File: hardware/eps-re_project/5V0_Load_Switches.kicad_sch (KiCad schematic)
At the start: 28 parts, among them U1 LMV321RIYLT, U10 SI2329DS-T1-GE3, U4 INA199C1DCKR, U5 NVTFS5116PLWFTAG, U6 NVTFS5116PLWFTAG, U7 NVTFS5116PLWFTAG, U8 SI2329DS-T1-GE3, U9 SI2329DS-T1-GE3

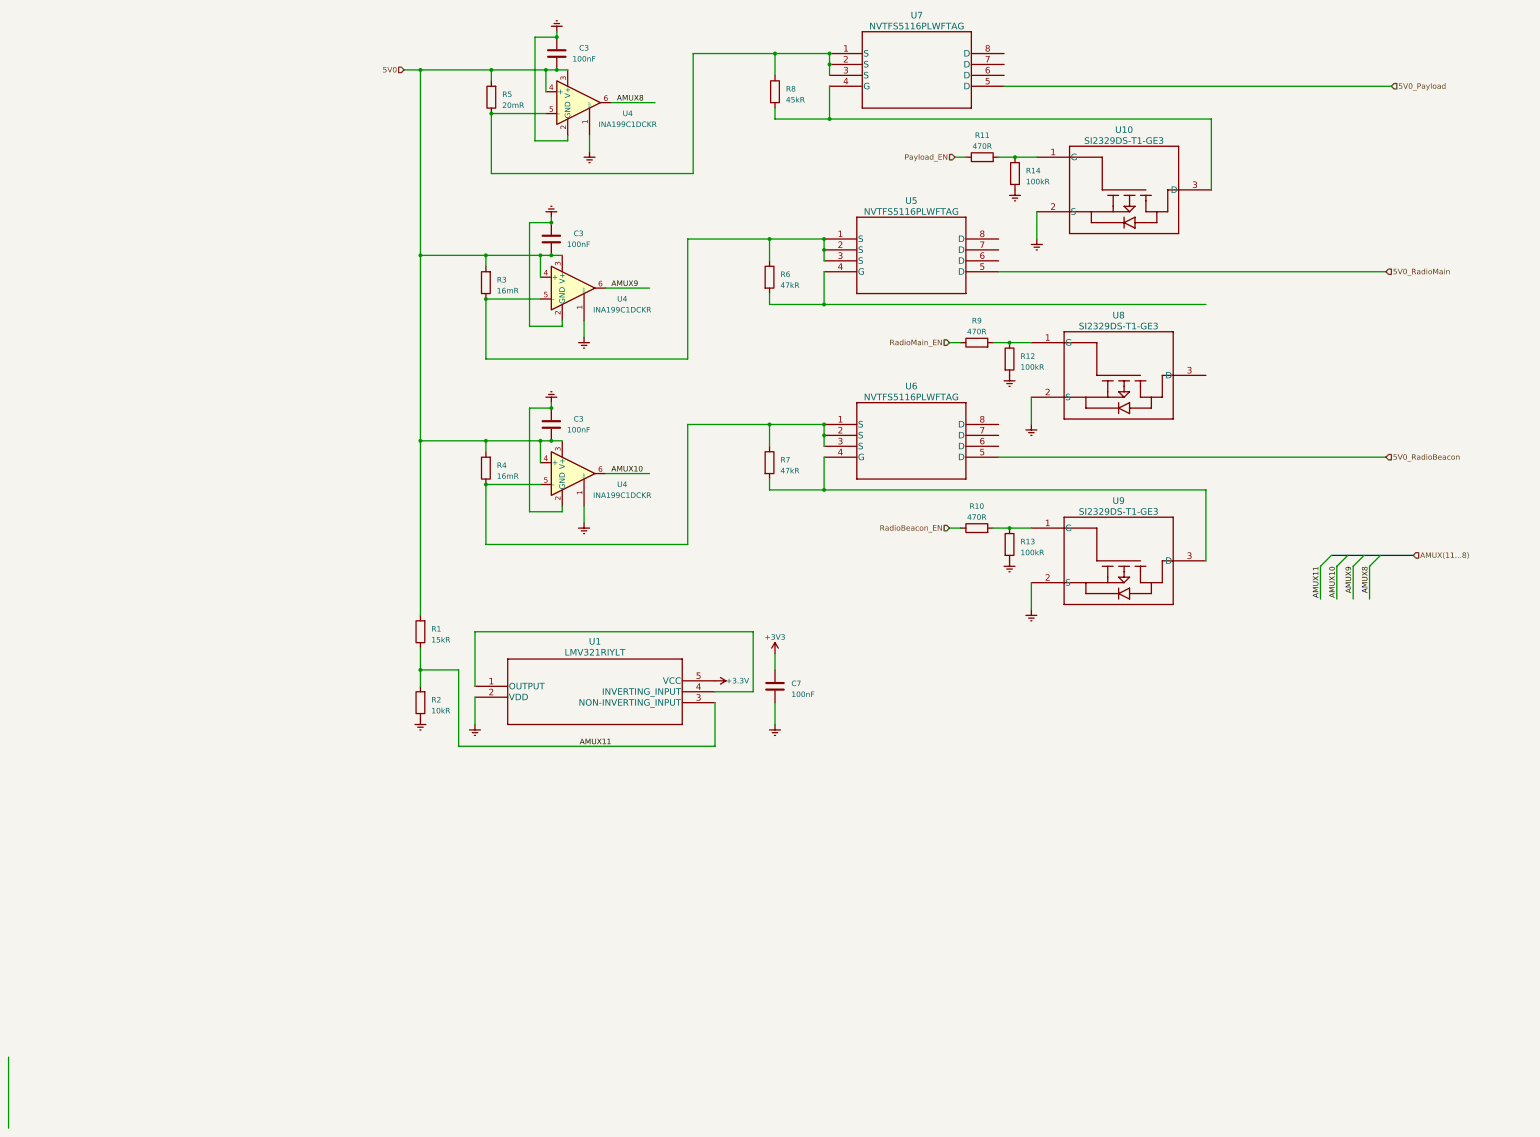
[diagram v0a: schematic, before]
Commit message: hardware: Restructuring the circuit, modifying symbols, footprints and other corrections
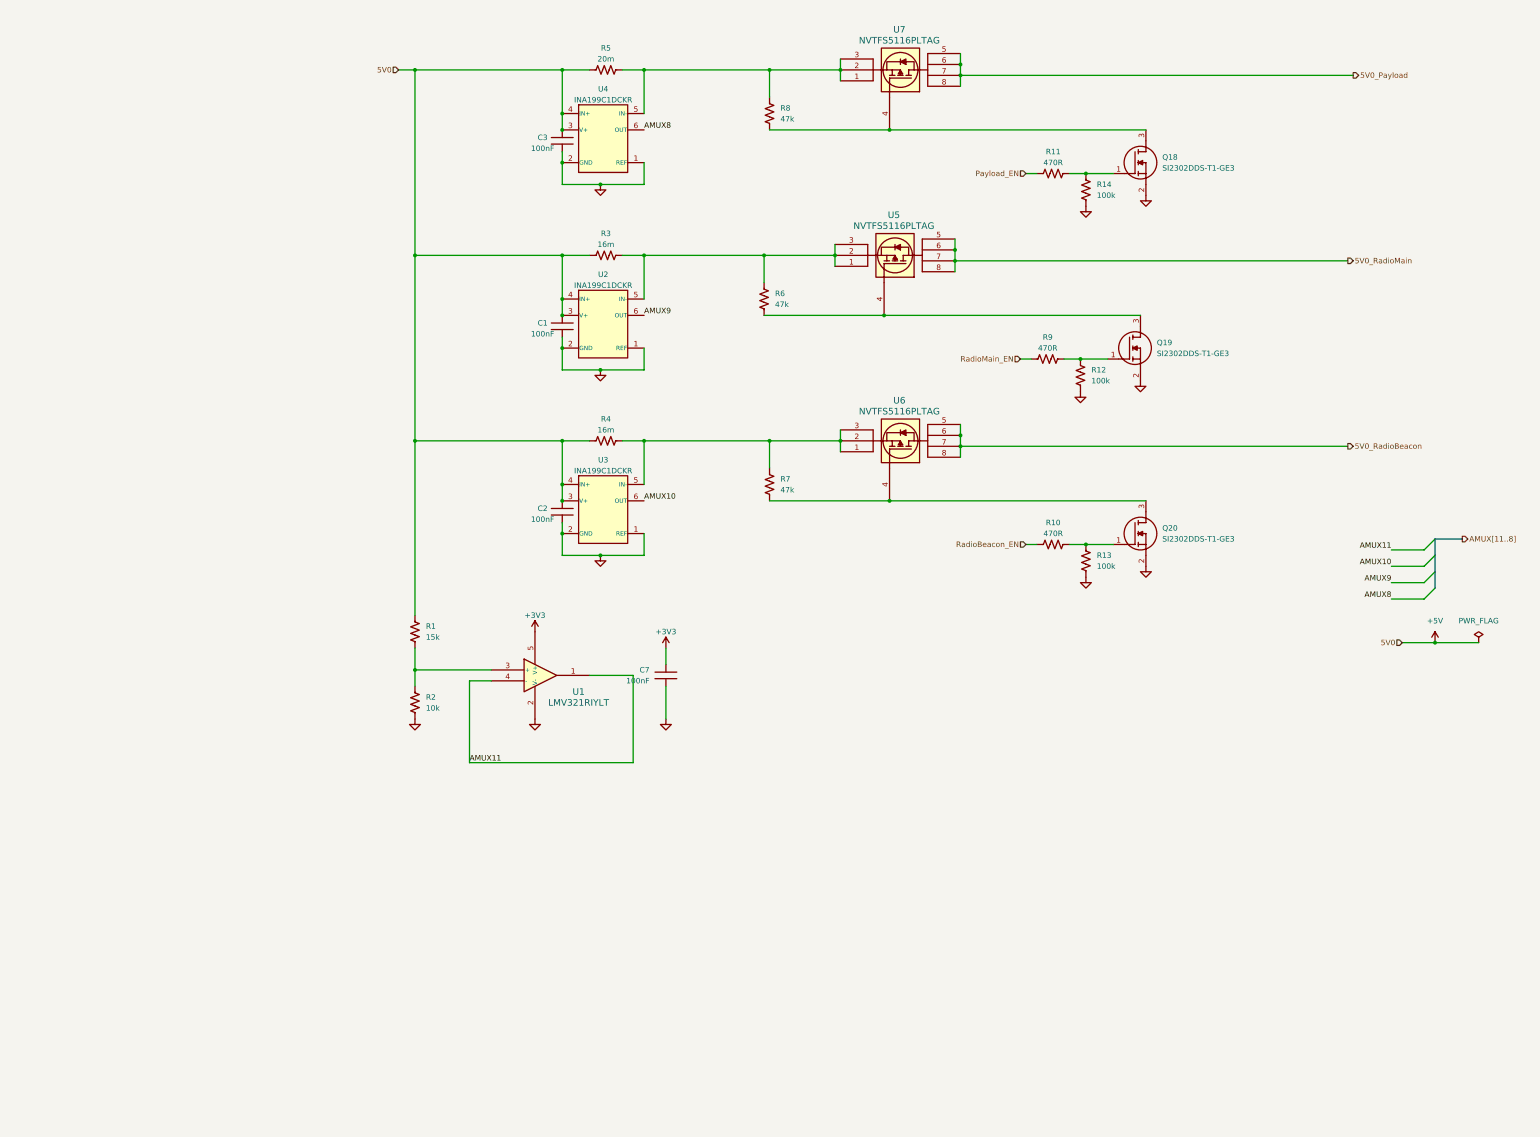
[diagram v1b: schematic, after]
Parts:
- removed C3 (x3), C7: 100nF, symbol Device:C
- removed R10, R11, R9: 470R, symbol Device:R
- removed R12, R13, R14: 100kR, symbol Device:R
- removed R3, R4: 16mR, symbol Device:R
- removed R5: 20mR, symbol Device:R
- removed R6, R7: 47kR, symbol Device:R
- removed R8: 45kR, symbol Device:R
- removed U10, U8, U9: SI2329DS-T1-GE3, SOT_DS-T1-GE3_VIS, symbol SI2329DS-T1-GE3:SI2329DS-T1-GE3
- removed U4 (x3): INA199C1DCKR, Package_TO_SOT_SMD:SOT-363_SC-70-6, symbol Amplifier_Current:INA199xxDCK
- removed U5, U6, U7: NVTFS5116PLWFTAG, WDFN8_3P30X3P30_ONS, symbol NVTFS5116PLWFTAG:NVTFS5116PLWFTAG
- added C1, C2, C3, C7: 100nF, footprints:C0603C104K5RACTU, symbol C0603C104K5RACTU:C0603C104K5RACTU
- added Q18, Q19, Q20: SI2302DDS-T1-GE3, footprints:SI2302DDS-T1-GE3, symbol SI2302DDS-T1-GE3:SI2302DDS-T1-GE3
- added R10, R11, R9: 470R, symbol Device:R_US
- added R12, R13, R14: 100k, symbol Device:R_US
- added R3, R4: 16m, symbol Device:R_US
- added R5: 20m, symbol Device:R_US
- added R6, R7, R8: 47k, symbol Device:R_US
- added U2, U3, U4: INA199C1DCKR, footprints:INA199C1DCKR, symbol INA199C1DCKR:INA199xxDCK
- added U5, U6, U7: NVTFS5116PLTAG, footprints:NVTFS5116PLTAG, symbol NVTFS5116PLWFTAG:NVTFS5116PLTAG
- R1: value 15kR -> 15k; symbol Device:R -> Device:R_US
- R2: value 10kR -> 10k; symbol Device:R -> Device:R_US
- U1: footprint SOT23-5_STM -> footprints:LMV321RIYLT
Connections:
- net +3.3V is gone; now on net +3V3: U1.5 (V+)
- net +3V3: now also C7.1
- net 5V0_Payload: now also U7.5, U7.6, U7.7, U7.8
- net 5V0_RadioBeacon: now also U6.5, U6.6, U6.7, U6.8
- net 5V0_RadioMain: now also U5.5, U5.6, U5.7, U5.8
- net AMUX10: now also U3.6 (OUT)
- net AMUX11: now also U1.1, U1.4 (-); no longer R1.1, R2.2, U1.3 (NON-INVERTING_INPUT)
- net AMUX8: now also U4.6 (OUT)
- net AMUX9: now also U2.6 (OUT)
- net Payload_EN: now also R11.1
- net RadioBeacon_EN: now also R10.1
- net RadioMain_EN: now also R9.1
- net 5V0 renamed +5V
- net +5V: now also C1.1, C2.1, C3.1, R3.2, R4.2, R5.2, U2.3 (V+), U2.4 (IN+), U3.3 (V+), U3.4 (IN+), U4.3 (V+), U4.4 (IN+)
- net Earth renamed GND
- net GND: now also C1.2, C2.2, C3.2, C7.2, Q18.2 (S), Q19.2 (S), Q20.2 (S), R12.2, R13.2, R14.2, U2.1 (REF), U2.2 (GND), U3.1 (REF), U3.2 (GND), U4.1 (REF), U4.2 (GND)
- new net: R4.1, R7.1, U3.5 (IN-), U6.1, U6.2, U6.3
- new net: Q20.3 (D), R7.2, U6.4
- new net: R3.1, R6.1, U2.5 (IN-), U5.1, U5.2, U5.3
- new net: R1.1, R2.2, U1.3 (+)
- new net: Q19.3 (D), R6.2, U5.4
- new net: R5.1, R8.1, U4.5 (IN-), U7.1, U7.2, U7.3
- new net: Q18.3 (D), R8.2, U7.4
- new net: Q20.1 (G), R10.2, R13.1
- new net: Q18.1 (G), R11.2, R14.1
- new net: Q19.1 (G), R12.1, R9.2
